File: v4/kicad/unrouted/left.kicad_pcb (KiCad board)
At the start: 2 copper layers, 160 x 118.6 mm, 67 parts

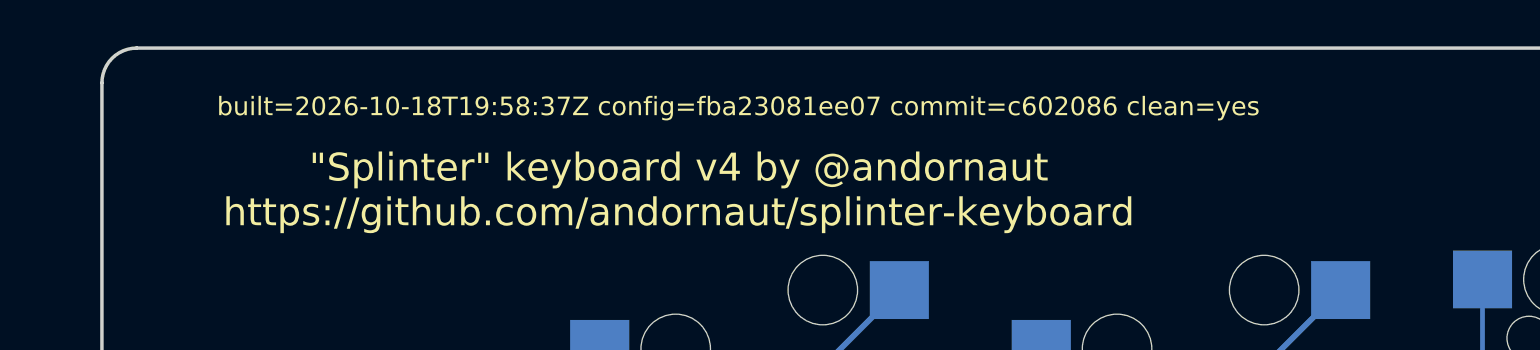
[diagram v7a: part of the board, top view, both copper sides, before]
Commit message: Have JLCPCB place the v4 reset switch
- Add sw_skqgabe010, a fork of ergogen's button footprint whose module layer
  follows `side`, so the position file reports the back-side reset switch on
  the Bottom instead of the bare Top. Pads and silk are unchanged.
- Assign C115351 (ALPS SKQGABE010) in jlcpcb-parts.json at rotation 0: the
  footprint matches JLCPCB's KEY-SMD_4P-L5.2-W5.2-P3.70-LS6.4 at 0 degrees.
- Move the reset switch from hand-soldered to placed by JLCPCB in the v4
  fabrication docs.
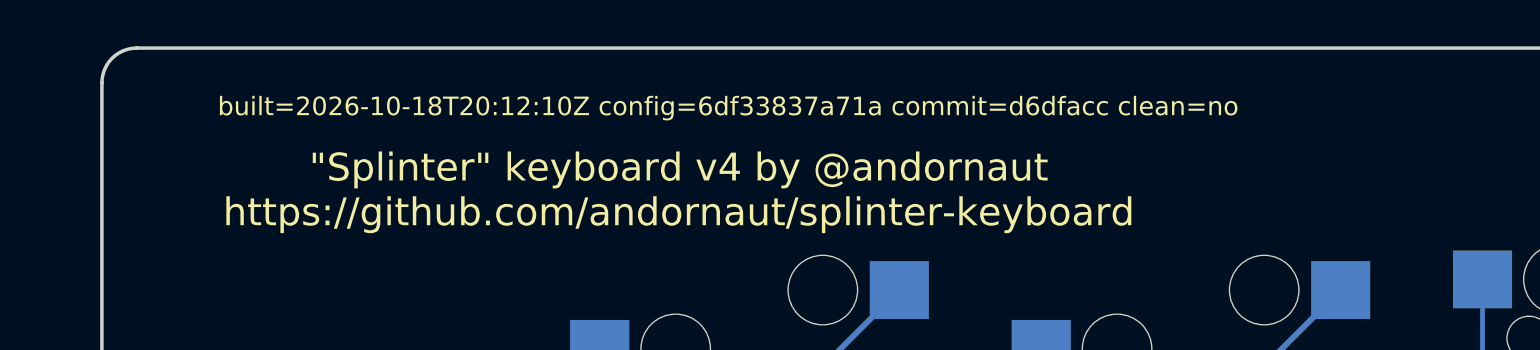
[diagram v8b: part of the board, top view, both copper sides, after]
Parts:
- B1: moved to B.Cu
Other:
- board text added: "built=2026-10-18T20:12:10Z config=6df33837a71a commit=d6dfacc clean=no"
- board text removed: "built=2026-10-18T19:58:37Z config=fba23081ee07 commit=c602086 clean=yes"
